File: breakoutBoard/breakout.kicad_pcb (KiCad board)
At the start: 2 copper layers, 62 x 106.9 mm, 9 parts, among them P1 CONN_02X50, P2 CONN_02X50, P3 CONN_02X50, P4 CONN_02X50, P7 CONN_02X30

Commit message: Basic pinout done and start of routing
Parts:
- added J1: Power_Breakout, Pin_Headers:Pin_Header_Straight_1x09_Pitch2.54mm, F.Cu at (84.0, 98.7)
- added J2: MIO_Breakout, Pin_Headers:Pin_Header_Straight_1x12_Pitch2.54mm, F.Cu at (84.3, 159.4)
- added J3: USB_OTG_Breakout, Pin_Headers:Pin_Header_Straight_1x06_Pitch2.54mm, F.Cu at (123.5, 65.7)
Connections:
- net /AD9361_AUXAC1 renamed Net-(P4-Pad7)
- net /AD9361_AUXAC2 renamed Net-(P4-Pad9)
- net /AD9361_AUXADC renamed Net-(P4-Pad8)
- net /AD9361_CLK renamed Net-(P4-Pad64)
- net /AD9361_GPO0 renamed Net-(P4-Pad2)
- net /AD9361_GPO1 renamed Net-(P4-Pad1)
- net /AD9361_GPO2 renamed Net-(P4-Pad4)
- net /AD9361_GPO3 renamed Net-(P4-Pad3)
- net /CAM_CLK_P renamed Net-(P1-Pad81)
- net /CAM_DATA0_P renamed Net-(P1-Pad54)
- net /CAM_DATA1_N renamed Net-(P1-Pad14)
- net /CAM_DATA2_N renamed Net-(P1-Pad13)
- net /CAM_DATA3_N renamed Net-(P1-Pad20)
- net /CAM_DATA4_N renamed Net-(P1-Pad19)
- net /CAM_DATA5_N renamed Net-(P1-Pad26)
- net /CAM_DATA6_N renamed Net-(P1-Pad25)
- net /CAM_GPIO_0 renamed Net-(P4-Pad20)
- net /CAM_GPIO_2 renamed Net-(P4-Pad19)
- net /CAM_GPIO_4 renamed Net-(P4-Pad26)
- net /CAM_GPIO_6 renamed Net-(P4-Pad25)
- net /CAM_GPIO_8 renamed Net-(P4-Pad32)
- net /CAM_REFCLK renamed Net-(P1-Pad82)
- net /CAM_SPI_CLK renamed Net-(P1-Pad31)
- net /CAM_SPI_MOSI renamed Net-(P1-Pad37)
- net /CAM_SYNC_P renamed Net-(P1-Pad47)
- net /CFG_INIT__B renamed Net-(P2-Pad10)
- net /CFG_VBATT renamed Net-(P1-Pad8)
- net /DIP_GPIO_1 renamed Net-(P4-Pad14)
- net /DIP_GPIO_3 renamed Net-(P2-Pad14)
- net /ET1_RXD3 renamed Net-(P4-Pad48)
- net /ETH0_MD1_N renamed Net-(P3-Pad54)
- net /ETH0_MD2_N renamed Net-(P3-Pad53)
- net /ETH0_PHY_LED0 renamed Net-(P3-Pad48)
- net /ETH0_PHY_LED1 renamed Net-(P3-Pad47)
- net /ETH1_RESETN renamed Net-(P4-Pad99)
- net /ETH1_RXD1 renamed Net-(P4-Pad43)
- net /ETH1_RX_CTRL renamed Net-(P4-Pad47)
- net /ETH1_TXD1 renamed Net-(P4-Pad53)
- net /ETH1_TX_CTRL renamed Net-(P4-Pad54)
- net /FAN_PWM renamed Net-(P4-Pad67)
- net /FAN_TACH renamed Net-(P4-Pad69)
- net /FMC_CLK0_M2C_N renamed Net-(P3-Pad94)
- net /FMC_CLK0_M2C_P renamed Net-(P3-Pad92)
- net /FMC_CLK1_M2C_N renamed Net-(P2-Pad44)
- net /FMC_CLK1_M2C_P renamed Net-(P2-Pad42)
- net /FMC_GBT_REFCLK_P renamed Net-(P1-Pad88)
- net /FMC_GBT_RX_P renamed Net-(P1-Pad87)
- net /FMC_GBT_TX_N renamed IO_00_33_JX1
- net /FMC_LA00_CC_N renamed Net-(P3-Pad87)
- net /FMC_LA01_CC_N renamed Net-(P3-Pad88)
- net /FMC_LA02_P renamed IO_L18_33_JX1_N
- net /FMC_LA03_P renamed Net-(P3-Pad26)
- net /FMC_LA04_P renamed IO_L20_33_JX1_N
- net /FMC_LA05_P renamed Net-(P3-Pad32)
- net /FMC_LA06_N renamed Net-(P3-Pad43)
- net /FMC_LA06_P renamed Net-(P3-Pad41)
- net /FMC_LA09_N renamed Net-(P3-Pad75)
- net /FMC_LA09_P renamed Net-(P3-Pad73)
- net /FMC_LA10_N renamed Net-(P3-Pad82)
- net /FMC_LA11_N renamed Net-(P3-Pad81)
- net /FMC_LA12_N renamed Net-(P3-Pad93)
- net /FMC_LA12_P renamed Net-(P3-Pad91)
- net /FMC_LA13_N renamed Net-(P3-Pad100)
- net /FMC_LA13_P renamed Net-(P3-Pad98)
- net /FMC_LA14_N renamed Net-(P3-Pad99)
- net /FMC_LA14_P renamed Net-(P3-Pad97)
- net /FMC_LA16_P renamed Net-(P2-Pad82)
- net /FMC_LA17_CC_N renamed Net-(P2-Pad37)
- net /FMC_LA17_CC_P renamed Net-(P2-Pad35)
- net /FMC_LA18_CC_N renamed Net-(P2-Pad38)
- net /FMC_LA18_CC_P renamed Net-(P2-Pad36)
- net /FMC_LA19_N renamed GPO_3
- net /FMC_LA19_P renamed GPO_1
- net /FMC_LA20_N renamed GPO_2
- net /FMC_LA20_P renamed GPO_0
- net /FMC_LA21_N renamed Net-(P2-Pad8)
- net /FMC_LA22_N renamed Net-(P2-Pad7)
- net /FMC_LA23_N renamed Net-(P2-Pad19)
- net /FMC_LA24_N renamed Net-(P2-Pad26)
- net /FMC_LA25_N renamed Net-(P2-Pad25)
- net /FMC_LA26_N renamed Net-(P2-Pad32)
- net /FMC_LA27_N renamed Net-(P2-Pad31)
- net /FMC_LA28_N renamed Net-(P2-Pad43)
- net /FMC_LA28_P renamed Net-(P2-Pad41)
- net /FMC_LA29_P renamed Net-(P2-Pad48)
- net /FMC_LA30_P renamed Net-(P2-Pad47)
- net /FMC_LA31_P renamed Net-(P2-Pad54)
- net /FMC_LA32_P renamed Net-(P2-Pad53)
- net /FMC_LA33_N renamed Net-(P2-Pad64)
- net /FMC_PRSNT renamed Net-(P2-Pad13)
- net /FPGA_TDI renamed Net-(P1-Pad3)
- net /FPGA_TDO renamed Net-(P1-Pad4)
- net /GPIO3 renamed Net-(P4-Pad88)
- net /HDMI_CLK renamed Net-(P1-Pad73)
- net /HDMI_D20 renamed Net-(P1-Pad41)
- net /HDMI_D21 renamed Net-(P1-Pad43)
- net /HDMI_D22 renamed Net-(P1-Pad48)
- net /HDMI_D24 renamed Net-(P1-Pad53)
- net /HDMI_D27 renamed Net-(P1-Pad64)
- net /HDMI_D34 renamed Net-(P1-Pad74)
- net /HDMI_D35 renamed Net-(P1-Pad76)
- net /HDMI_DE renamed Net-(P1-Pad75)
- net /HDMI_HSYNC renamed Net-(P1-Pad44)
- net /HDMI_PD renamed Net-(P1-Pad10)
- net /HDMI_SPDIF renamed Net-(P1-Pad36)
- net /HDMI_SPDIF_OUT renamed Net-(P1-Pad38)
- net /HDMI_VSYNC renamed Net-(P1-Pad42)
- net /I2C3_SCL renamed Net-(P2-Pad76)
- net /I2C3_SDA renamed Net-(P2-Pad74)
- net /I2S_LRCLK renamed Net-(P4-Pad36)
- net /I2S_MCLK renamed Net-(P4-Pad31)
- net /I2S_SDATA_IN renamed Net-(P4-Pad35)
- net /I2S_SDATA_OUT renamed Net-(P4-Pad38)
- net /JTAG_TCK renamed Net-(P1-Pad2)
- net /JTAG_TMS renamed Net-(P1-Pad1)
- net /LED_GPIO_0 renamed Net-(P4-Pad70)
- net /LED_GPIO_1 renamed Net-(P4-Pad13)
- net /MGTREFCLK1_N renamed JTAG_TDO
- net /MGTREFCLK1_P renamed JTAG_TCK
- net /MGTRX2_N renamed Net-(P1-Pad93)
- net /MGTRX2_P renamed Net-(P1-Pad91)
- net /MGTTX2_P renamed IO_L16_33_JX1_N
- net /PB_GPIO_1 renamed Net-(P4-Pad37)
- net /PB_GPIO_2 renamed Net-(P4-Pad42)
- net /PB_GPIO_3 renamed Net-(P4-Pad44)
- net /RF_GPIO1_BANK13 renamed Net-(P2-Pad63)
- net /RF_GPIO4_BANK34 renamed Net-(P4-Pad63)
- net /RF_GPIO5_BANK34 renamed Net-(P4-Pad68)
- net /SD1_B_CDN renamed Net-(P3-Pad42)
- net /SD1_B_CLK renamed Net-(P3-Pad44)
- net /SD1_B_DAT0 renamed Net-(P3-Pad38)
- net /SD1_B_DAT1 renamed IO_L01_33_JX1_P
- net /SD1_B_DAT3 renamed IO_L01_33_JX1_N
- net /SDA renamed Net-(P2-Pad20)
- net /SFP_GBT_RX_N renamed Net-(P1-Pad94)
- net /SFP_GBT_RX_P renamed Net-(P1-Pad92)
- net /SFP_GBT_TX_P renamed Net-(P3-Pad14)
- net /SGPIO1 renamed Net-(P4-Pad87)
- net /SGPIO3 renamed Net-(P4-Pad94)
- net /SGPIO_1 renamed Net-(P7-Pad25)
- net /SGPIO_3 renamed Net-(P7-Pad29)
- net /SGPIO_4 renamed Net-(P7-Pad32)
- net /SPI2_NSS renamed Net-(P4-Pad73)
- net /SYS_SPI_MISO renamed Net-(P4-Pad74)
- net /SYS_SPI_MOSI renamed Net-(P2-Pad75)
- net /SYS_SPI_NSS renamed Net-(P4-Pad76)
- net /SYS_SPI_SCK renamed Net-(P2-Pad73)
- net /USB_OTG_CPEN renamed Net-(P3-Pad69)
- net /USB_OTG_ID renamed Net-(P3-Pad64)
- net /USB_UART_RXD renamed Net-(P4-Pad100)
- net /USB_UART_TXD renamed Net-(P4-Pad97)
- net /USB_VBUS_OTG renamed Net-(P3-Pad67)
- net /VCCIO_EN renamed Net-(P2-Pad9)
- net Net-(P3-Pad2) renamed JTAG_TMS
- net Net-(P3-Pad4) renamed JTAG_TDI
- P1 pad 11: /CAM_DATA2_P -> JX_MGTAVCC
- P1 pad 12: /CAM_DATA1_P -> GND
- P1 pad 15: GND -> Net-(P1-Pad15)
- P1 pad 16: GND -> Net-(P1-Pad16)
- P1 pad 17: /CAM_DATA4_P -> GND
- P1 pad 18: /CAM_DATA3_P -> GND
- P1 pad 21: GND -> Net-(P1-Pad21)
- P1 pad 22: GND -> Net-(P1-Pad22)
- P1 pad 23: /CAM_DATA6_P -> GND
- P1 pad 24: /CAM_DATA5_P -> GND
- P1 pad 27: GND -> Net-(P1-Pad27)
- P1 pad 28: GND -> Net-(P1-Pad28)
- P1 pad 29: /CAM_SPI_EN -> GND
- P1 pad 30: /CAM_DATA7_P -> JX_MGTAVTT
- P1 pad 32: /CAM_DATA7_N -> JX_MGTAVTT
- P1 pad 33: GND -> Net-(P1-Pad33)
- P1 pad 34: GND -> Net-(P1-Pad34)
- P1 pad 35: /CAM_SPI_MISO -> GND
- P1 pad 39: GND -> Net-(P1-Pad39)
- P1 pad 45: GND -> JX_VCCO_13
- P1 pad 46: GND -> JX_VCCO_13
- P1 pad 49: /CAM_SYNC_N -> GND
- P1 pad 5: /RSTN_C2M -> JX_MGTAVCC
- P1 pad 50: /HDMI_D23 -> GND
- P1 pad 51: GND -> Net-(P1-Pad51)
- P1 pad 52: GND -> Net-(P1-Pad52)
- P1 pad 55: /HDMI_D25 -> GND
- P1 pad 56: /CAM_DATA0_N -> GND
- P1 pad 57: /VIN_HDR -> Net-(P1-Pad57)
- P1 pad 58: /VIN_HDR -> Net-(P1-Pad58)
- P1 pad 59: /VIN_HDR -> Net-(P1-Pad59)
- P1 pad 6: /PWR_ENABLE -> GND
- P1 pad 60: /VIN_HDR -> Net-(P1-Pad60)
- P1 pad 61: /HDMI_D28 -> GND
- P1 pad 62: /HDMI_D26 -> GND
- P1 pad 63: /HDMI_D29 -> USB_ID
- P1 pad 66: GND -> Net-(P1-Pad66)
- P1 pad 67: /HDMI_D32 -> USB_OTG_P
- P1 pad 68: /HDMI_D30 -> USB_VBUS_OTG
- P1 pad 69: /HDMI_D33 -> USB_OTG_N
- P1 pad 7: /CFG_DONE -> JX_MGTAVCC
- P1 pad 70: /HDMI_D31 -> USB_OTG_CPEN
- P1 pad 77: /VADJ -> GND
- P1 pad 79: /VADJ -> Net-(P1-Pad79)
- P1 pad 80: /VADJ -> Net-(P1-Pad80)
- P1 pad 83: /CAM_CLK_N -> GND
- P1 pad 84: /PB_GPIO_0 -> GND
- P1 pad 85: GND -> Net-(P1-Pad85)
- P1 pad 86: GND -> Net-(P1-Pad86)
- P1 pad 89: /FMC_GBT_RX_N -> GND
- P1 pad 9: /HDMI_INTN -> JX_MGTAVCC
- P1 pad 90: /FMC_GBT_REFCLK_N -> GND
- P2 pad 100: /DIP_GPIO_0 -> MIO51
- P2 pad 11: /VIN_HDR -> GND
- P2 pad 12: /PG_MODULE -> GND
- P2 pad 15: GND -> Net-(P2-Pad15)
- P2 pad 16: GND -> Net-(P2-Pad16)
- P2 pad 17: /FMC_LA23_P -> GND
- P2 pad 18: /SCL -> GND
- P2 pad 21: GND -> Net-(P2-Pad21)
- P2 pad 22: GND -> Net-(P2-Pad22)
- P2 pad 23: /FMC_LA25_P -> GND
- P2 pad 24: /FMC_LA24_P -> GND
- P2 pad 27: GND -> Net-(P2-Pad27)
- P2 pad 28: GND -> Net-(P2-Pad28)
- P2 pad 29: /FMC_LA27_P -> GND
- P2 pad 30: /FMC_LA26_P -> GND
- P2 pad 33: GND -> Net-(P2-Pad33)
- P2 pad 34: GND -> Net-(P2-Pad34)
- P2 pad 45: GND -> Net-(P2-Pad45)
- P2 pad 46: GND -> Net-(P2-Pad46)
- P2 pad 49: /FMC_LA30_N -> GND
- P2 pad 5: /FMC_LA22_P -> GND
- P2 pad 50: /FMC_LA29_N -> GND
- P2 pad 51: GND -> Net-(P2-Pad51)
- P2 pad 52: GND -> Net-(P2-Pad52)
- P2 pad 55: /FMC_LA32_N -> GND
- P2 pad 56: /FMC_LA31_N -> GND
- P2 pad 57: /VIN_HDR -> Net-(P2-Pad57)
- P2 pad 58: /VIN_HDR -> Net-(P2-Pad58)
- P2 pad 59: /VIN_HDR -> Net-(P2-Pad59)
- P2 pad 6: /FMC_LA21_P -> GND
- P2 pad 60: /VIN_HDR -> Net-(P2-Pad60)
- P2 pad 61: /RF_GPIO0_BANK13 -> GND
- P2 pad 62: /FMC_LA33_P -> GND
- P2 pad 67: /I2C2_SDA -> Net-(P2-Pad67)
- P2 pad 68: /I2C2_SDA -> Net-(P2-Pad68)
- P2 pad 69: /I2C2_SCL -> Net-(P2-Pad69)
- P2 pad 70: /I2C2_SCL -> Net-(P2-Pad70)
- P2 pad 77: /1V8 -> Net-(P2-Pad77)
- P2 pad 78: GND -> Net-(P2-Pad78)
- P2 pad 79: /1V8 -> Net-(P2-Pad79)
- P2 pad 80: /1V8 -> Net-(P2-Pad80)
- P2 pad 81: /FMC_LA15_P -> 3V3_I2C
- P2 pad 83: /FMC_LA15_N -> GND
- P2 pad 84: /FMC_LA16_N -> GND
- P2 pad 85: GND -> MIO15
- P2 pad 86: GND -> MIO12
- P2 pad 87: /SFP_GPIO_0 -> MIO10
- P2 pad 88: /SFP_GPIO_2 -> MIO11
- P2 pad 89: /SFP_GPIO_1 -> GND
- P2 pad 90: /SFP_GPIO_3 -> GND
- P2 pad 91: GND -> MIO13
- P2 pad 92: GND -> MIO46
- P2 pad 93: /SFP_GPIO_6 -> MIO14
- P2 pad 94: /SFP_GPIO_4 -> MIO47
- P2 pad 95: /RF_GPIO2_BANK12 -> GND
- P2 pad 96: /SFP_GPIO_5 -> GND
- P2 pad 97: /VADJ -> MIO0
- P2 pad 98: /LED_GPIO_3 -> MIO49
- P2 pad 99: Net-(P2-Pad99) -> MIO48
- P3 pad 10: /1V0_AVCC -> Net-(P3-Pad10)
- P3 pad 11: GND -> IO_L16_33_JX1_P
- P3 pad 12: /1V0_AVCC -> Net-(P3-Pad12)
- P3 pad 15: /MGTTX2_N -> GND
- P3 pad 16: /SFP_GBT_TX_N -> GND
- P3 pad 17: GND -> IO_L18_33_JX1_P
- P3 pad 18: GND -> Net-(P3-Pad18)
- P3 pad 21: /FMC_LA02_N -> GND
- P3 pad 22: Net-(P3-Pad22) -> GND
- P3 pad 23: GND -> IO_L20_33_JX1_P
- P3 pad 24: GND -> Net-(P3-Pad24)
- P3 pad 27: /FMC_LA04_N -> GND
- P3 pad 28: /FMC_LA03_N -> GND
- P3 pad 29: /1V2_AVTT -> IO_L22_33_JX1_P
- P3 pad 30: GND -> Net-(P3-Pad30)
- P3 pad 31: /1V2_AVTT -> IO_L22_33_JX1_N
- P3 pad 33: /SD1_B_CMD -> GND
- P3 pad 34: /FMC_LA05_N -> GND
- P3 pad 36: GND -> Net-(P3-Pad36)
- P3 pad 40: /SD1_B_DAT2 -> GND
- P3 pad 45: /VADJ -> GND
- P3 pad 46: /VADJ -> GND
- P3 pad 49: GND -> Net-(P3-Pad49)
- P3 pad 5: GND -> PWR_ENABLE
- P3 pad 50: GND -> Net-(P3-Pad50)
- P3 pad 51: /ETH0_MD2_P -> GND
- P3 pad 52: /ETH0_MD1_P -> GND
- P3 pad 55: GND -> Net-(P3-Pad55)
- P3 pad 56: GND -> Net-(P3-Pad56)
- P3 pad 57: /ETH0_MD4_P -> +5V
- P3 pad 58: /ETH0_MD3_P -> +5V
- P3 pad 59: /ETH0_MD4_N -> +5V
- P3 pad 6: /1V0_AVCC -> Carrier_Reset
- P3 pad 60: /ETH0_MD3_N -> +5V
- P3 pad 61: GND -> Net-(P3-Pad61)
- P3 pad 62: GND -> Net-(P3-Pad62)
- P3 pad 63: /FMC_LA07_P -> Net-(P3-Pad63)
- P3 pad 65: /FMC_LA07_P -> GND
- P3 pad 68: /FMC_LA08_P -> Net-(P3-Pad68)
- P3 pad 7: /FMC_GBT_TX_P -> FPGA_VBATT
- P3 pad 70: /FMC_LA08_N -> Net-(P3-Pad70)
- P3 pad 74: /FMC_LA08_P -> Net-(P3-Pad74)
- P3 pad 76: /FMC_LA08_N -> Net-(P3-Pad76)
- P3 pad 78: GND -> JX_VCCO_12
- P3 pad 79: /FMC_LA11_P -> JX_VCCO_12
- P3 pad 8: /1V0_AVCC -> Net-(P3-Pad8)
- P3 pad 80: /FMC_LA10_P -> JX_VCCO_12
- P3 pad 83: GND -> Net-(P3-Pad83)
- P3 pad 84: GND -> Net-(P3-Pad84)
- P3 pad 85: /FMC_LA00_CC_P -> GND
- P3 pad 86: /FMC_LA01_CC_P -> GND
- P3 pad 89: GND -> Net-(P3-Pad89)
- P3 pad 90: GND -> Net-(P3-Pad90)
- P4 pad 11: GND -> Net-(P4-Pad11)
- P4 pad 12: GND -> +5V
- P4 pad 15: /LED_GPIO_2 -> GND
- P4 pad 16: /DIP_GPIO_2 -> GND
- P4 pad 17: GND -> Net-(P4-Pad17)
- P4 pad 18: GND -> Net-(P4-Pad18)
- P4 pad 21: /CAM_GPIO_3 -> GND
- P4 pad 22: /CAM_GPIO_1 -> GND
- P4 pad 23: GND -> Net-(P4-Pad23)
- P4 pad 24: GND -> Net-(P4-Pad24)
- P4 pad 27: /CAM_GPIO_7 -> GND
- P4 pad 28: /CAM_GPIO_5 -> GND
- P4 pad 29: GND -> Net-(P4-Pad29)
- P4 pad 30: GND -> Net-(P4-Pad30)
- P4 pad 33: /I2S_BCLK -> GND
- P4 pad 34: /RF_GPIO3_BANK34 -> GND
- P4 pad 41: /ETH1_RX_CLK -> Net-(P4-Pad41)
- P4 pad 45: /ETH1_RX_CLK -> GND
- P4 pad 46: /ETH1_RXD2 -> GND
- P4 pad 49: GND -> Net-(P4-Pad49)
- P4 pad 5: GND -> Net-(P4-Pad5)
- P4 pad 50: GND -> Net-(P4-Pad50)
- P4 pad 51: /ETH1_TXD0 -> GND
- P4 pad 52: /ETH1_TX_CLK -> GND
- P4 pad 55: GND -> Net-(P4-Pad55)
- P4 pad 56: GND -> Net-(P4-Pad56)
- P4 pad 57: /ETH1_MDC -> +5V
- P4 pad 58: /ETH1_TXD2 -> +5V
- P4 pad 59: /ETH1_MDIO -> +5V
- P4 pad 6: GND -> Net-(P4-Pad6)
- P4 pad 60: /EHT1_TXD3 -> +5V
- P4 pad 61: GND -> Net-(P4-Pad61)
- P4 pad 62: GND -> Net-(P4-Pad62)
- P4 pad 75: /SPI2_MISO -> Net-(P4-Pad75)
- P4 pad 77: /GPIO0 -> GND
- P4 pad 78: /SPI2_SCK -> JX_VCCO_33_34
- P4 pad 79: /GPIO1 -> JX_VCCO_33_34
- P4 pad 80: /SPI2_MOSI -> JX_VCCO_33_34
- P4 pad 83: GND -> Net-(P4-Pad83)
- P4 pad 84: GND -> Net-(P4-Pad84)
- P4 pad 85: /SGPIO0 -> GND
- P4 pad 86: /GPIO2 -> GND
- P4 pad 89: GND -> Net-(P4-Pad89)
- P4 pad 90: GND -> Net-(P4-Pad90)
- P4 pad 91: /SYS_SDA -> GND
- P4 pad 92: /SGPIO2 -> GND
- P4 pad 93: /SYS_SCL -> Net-(P4-Pad93)
- P4 pad 95: GND -> Net-(P4-Pad95)
- P4 pad 96: GND -> Net-(P4-Pad96)
- P4 pad 98: Net-(P4-Pad98) -> JX_VCCO_13
- P7 pad 1: GND -> +5V
- P7 pad 10: /SYS_SDA -> GND
- P7 pad 11: +3V3 -> Net-(P7-Pad11)
- P7 pad 13: GND -> Net-(P7-Pad13)
- P7 pad 14: +3V3 -> GND
- P7 pad 15: /SPI2_MISO -> Net-(P7-Pad15)
- P7 pad 17: GND -> +5V
- P7 pad 18: /SPI2_MOSI -> GND
- P7 pad 19: /SPI2_SCK -> Net-(P7-Pad19)
- P7 pad 2: +3V3 -> GND
- P7 pad 22: Net-(P7-Pad22) -> GND
- P7 pad 23: GND -> Net-(P7-Pad23)
- P7 pad 24: /SGPIO_0 -> GND
- P7 pad 27: GND -> Net-(P7-Pad27)
- P7 pad 28: /SGPIO_2 -> GND
- P7 pad 3: +5V -> PWR_ENABLE
- P7 pad 33: +3V3 -> GND
- P7 pad 34: GND -> MIO0
- P7 pad 36: +3V3 -> MIO48
- P7 pad 37: /SYS_MISO -> GND
- P7 pad 38: GND -> MIO10
- P7 pad 40: /SYS_MOSI -> MIO14
- P7 pad 41: /SYS_SCK -> GND
- P7 pad 42: GND -> MIO13
- P7 pad 44: /GPIO_7 -> +5V
- P7 pad 45: /GPIO_8 -> GND
- P7 pad 46: GND -> MIO15
- P7 pad 48: /GPIO_9 -> MIO51
- P7 pad 49: /GPIO_10 -> GND
- P7 pad 5: GND -> Net-(P7-Pad5)
- P7 pad 50: GND -> MIO49
- P7 pad 52: /GPIO_11 -> MIO47
- P7 pad 53: +3V3 -> GND
- P7 pad 54: GND -> MIO46
- P7 pad 56: +3V3 -> MIO11
- P7 pad 57: +5V -> GND
- P7 pad 58: GND -> MIO12
- P7 pad 6: +12V -> GND
- P7 pad 60: +12V -> +5V
- P7 pad 7: /SYS_SCL -> Net-(P7-Pad7)
- P7 pad 9: GND -> Net-(P7-Pad9)
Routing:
- net Net-(P3-Pad74): track 0.00 -> 0.93 mm
- net GND: track 0.00 -> 0.93 mm
- net /SD1_B_DAT2: track 0.93 -> 0.00 mm
- net /FMC_LA08_P: track 0.93 -> 0.00 mm
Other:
- board size 62 x 106.9 mm -> 78.5 x 106.9 mm

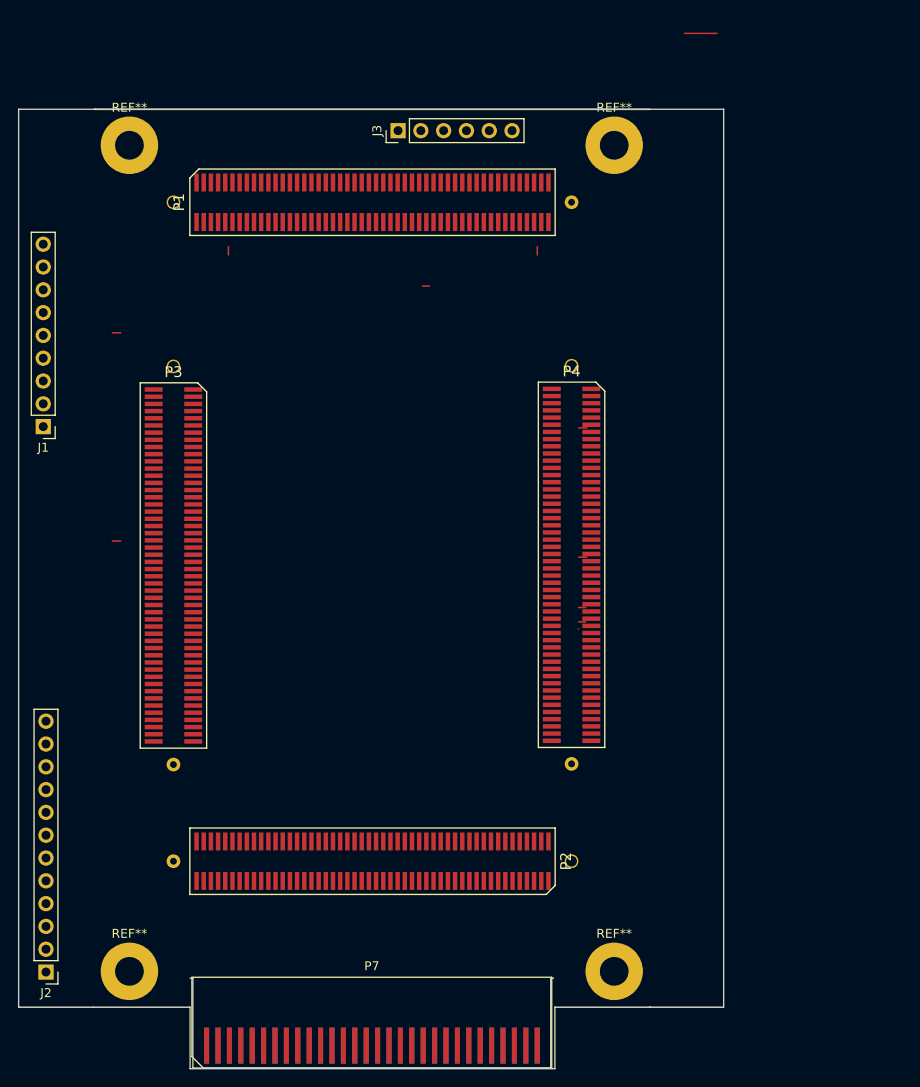
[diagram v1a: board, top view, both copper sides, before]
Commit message: Added zones
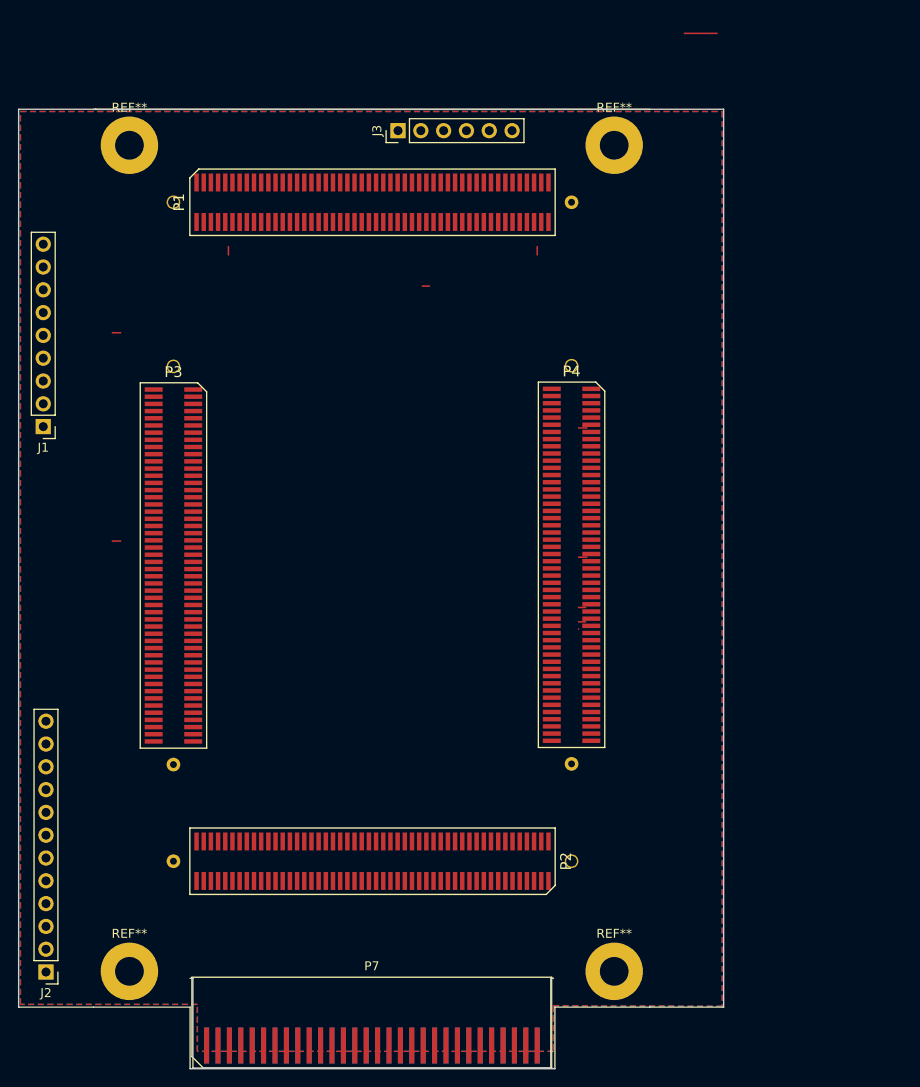
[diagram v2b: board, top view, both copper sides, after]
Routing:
- added copper zone on B.Cu, net +5V
- added copper zone on F.Cu, net GND
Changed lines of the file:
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@@
   (general
     (links 194)
-    (no_connects 194)
+    (no_connects 178)
     (area 89.510799 63.247199 151.636801 170.255001)
     (thickness 1.6)
@@
   (segment (start 97 111.4) (end 96.011767 111.4) (width 0.1778) (layer F.Cu) (net 184))
   (segment (start 96.069938 123.4) (end 97 123.4) (width 0.1778) (layer F.Cu) (net 202))
+  (zone (net 5) (net_name GND) (layer F.Cu) (hatch edge 0.508)
+    (connect_pads (clearance 0.508))
+    (min_thickness 0.254)
+    (fill yes (arc_segments 16) (thermal_gap 0.508) (thermal_bridge_width 0.508))
+    (polygon
+      (pts
+        (xy 159.6136 163.2204) (xy 140.8176 163.1696) (xy 140.8176 168.2496) (xy 101.1428 168.2496) (xy 101.1428 163.0172)
+        (xy 81.4324 163.0172) (xy 81.4324 63.5508) (xy 159.6136 63.5508)
+      )
+    )
+  )
+  (zone (net 10) (net_name +5V) (layer B.Cu) (hatch edge 0.508)
+    (connect_pads (clearance 0.508))
+    (min_thickness 0.254)
+    (fill yes (arc_segments 16) (thermal_gap 0.508) (thermal_bridge_width 0.508))
+    (polygon
+      (pts
+        (xy 159.6136 163.2204) (xy 140.8176 163.1696) (xy 140.8176 168.2496) (xy 101.1428 168.2496) (xy 101.1428 163.0172)
+        (xy 81.4324 163.0172) (xy 81.4324 63.5508) (xy 159.6136 63.5508)
+      )
+    )
+  )
 )

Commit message: Started routing
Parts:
- J1: footprint Pin_Headers:Pin_Header_Straight_1x09_Pitch2.54mm -> Pin_Headers:Pin_Header_Straight_1x10_Pitch2.54mm
- moved J2 28.2 mm to (84.9, 131.3), turned to 0 degrees
- moved J1 2.44 mm to (83.9, 101.1)
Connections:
- J2 pad 1: MIO15 -> MIO12
- J2 pad 10: MIO46 -> MIO14
- J2 pad 11: MIO11 -> MIO0
- J2 pad 12: MIO12 -> MIO48
- J2 pad 2: MIO10 -> MIO11
- J2 pad 3: MIO13 -> MIO46
- J2 pad 4: MIO14 -> MIO47
- J2 pad 5: MIO0 -> MIO49
- J2 pad 6: MIO48 -> MIO51
- J2 pad 7: MIO51 -> MIO15
- J2 pad 8: MIO49 -> MIO10
- J2 pad 9: MIO47 -> MIO13
- P7 pad 10: GND -> MIO49
- P7 pad 11: Net-(P7-Pad11) -> GND
- P7 pad 13: Net-(P7-Pad13) -> MIO14
- P7 pad 14: GND -> MIO47
- P7 pad 15: Net-(P7-Pad15) -> GND
- P7 pad 17: +5V -> MIO13
- P7 pad 18: GND -> MIO46
- P7 pad 19: Net-(P7-Pad19) -> GND
- P7 pad 2: GND -> +5V
- P7 pad 21: Net-(P7-Pad21) -> MIO10
- P7 pad 22: GND -> MIO11
- P7 pad 23: Net-(P7-Pad23) -> GND
- P7 pad 25: Net-(P7-Pad25) -> MIO15
- P7 pad 26: GND -> MIO12
- P7 pad 27: Net-(P7-Pad27) -> GND
- P7 pad 3: PWR_ENABLE -> GND
- P7 pad 30: GND -> Net-(P7-Pad30)
- P7 pad 32: Net-(P7-Pad32) -> GND
- P7 pad 33: GND -> +5V
- P7 pad 34: MIO0 -> +5V
- P7 pad 36: MIO48 -> GND
- P7 pad 37: GND -> Net-(P7-Pad37)
- P7 pad 38: MIO10 -> Net-(P7-Pad38)
- P7 pad 40: MIO14 -> GND
- P7 pad 41: GND -> Net-(P7-Pad41)
- P7 pad 42: MIO13 -> Net-(P7-Pad42)
- P7 pad 44: +5V -> GND
- P7 pad 45: GND -> Net-(P7-Pad45)
- P7 pad 46: MIO15 -> Net-(P7-Pad46)
- P7 pad 48: MIO51 -> GND
- P7 pad 49: GND -> Net-(P7-Pad49)
- P7 pad 5: Net-(P7-Pad5) -> MIO48
- P7 pad 50: MIO49 -> Net-(P7-Pad50)
- P7 pad 52: MIO47 -> GND
- P7 pad 53: GND -> Net-(P7-Pad53)
- P7 pad 54: MIO46 -> Net-(P7-Pad54)
- P7 pad 56: MIO11 -> GND
- P7 pad 57: GND -> PWR_ENABLE
- P7 pad 58: MIO12 -> Net-(P7-Pad58)
- P7 pad 6: GND -> MIO51
- P7 pad 60: +5V -> GND
- P7 pad 7: Net-(P7-Pad7) -> GND
- P7 pad 9: Net-(P7-Pad9) -> MIO0
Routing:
- net MIO12: track 0.00 -> 55.7 mm, vias 0 -> 1
- net MIO11: track 0.00 -> 53.2 mm, vias 0 -> 1
- net MIO46: track 0.00 -> 50.3 mm, vias 0 -> 1
- net MIO47: track 0.00 -> 47.2 mm, vias 0 -> 1
- net MIO15: track 0.00 -> 47.2 mm
- net MIO10: track 0.00 -> 46.4 mm
- net MIO13: track 0.00 -> 44.5 mm
- net MIO49: track 0.00 -> 44.2 mm, vias 0 -> 1
- net MIO14: track 0.00 -> 43.6 mm
- net MIO0: track 0.00 -> 42.3 mm
- net MIO51: track 0.00 -> 40.8 mm, vias 0 -> 1
- net MIO48: track 0.00 -> 37.6 mm
- net GND: track 0.93 -> 16.7 mm

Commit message: Work on schematic and traces
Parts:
- added J4: Cardedge breakout, Pin_Headers:Pin_Header_Straight_1x17_Pitch2.54mm, F.Cu at (176.8, 158.4)
- added P5: CONN_02X30, Connectors_Samtec:MECF-30-01-L-DV-WT_Socket, F.Cu at (163.9, 138.5)
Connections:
- net Net-(P2-Pad10) renamed AUXDAC2
- net Net-(P2-Pad7) renamed AUXADC
- net Net-(P2-Pad8) renamed AUXDAC1
- net Net-(P2-Pad9) renamed VDDA_GPO_PWR
- net Net-(P4-Pad10) renamed PG_1P8V
- P1 pad 1: Net-(P1-Pad1) -> GND
- P1 pad 10: Net-(P1-Pad10) -> GND
- P1 pad 100: Net-(P1-Pad100) -> GND
- P1 pad 13: Net-(P1-Pad13) -> GND
- P1 pad 14: Net-(P1-Pad14) -> GND
- P1 pad 15: Net-(P1-Pad15) -> GND
- P1 pad 16: Net-(P1-Pad16) -> GND
- P1 pad 19: Net-(P1-Pad19) -> GND
- P1 pad 2: Net-(P1-Pad2) -> GND
- P1 pad 20: Net-(P1-Pad20) -> GND
- P1 pad 21: Net-(P1-Pad21) -> GND
- P1 pad 22: Net-(P1-Pad22) -> GND
- P1 pad 25: Net-(P1-Pad25) -> GND
- P1 pad 26: Net-(P1-Pad26) -> GND
- P1 pad 27: Net-(P1-Pad27) -> GND
- P1 pad 28: Net-(P1-Pad28) -> GND
- P1 pad 3: Net-(P1-Pad3) -> GND
- P1 pad 31: Net-(P1-Pad31) -> GND
- P1 pad 33: Net-(P1-Pad33) -> GND
- P1 pad 34: Net-(P1-Pad34) -> GND
- P1 pad 36: Net-(P1-Pad36) -> GND
- P1 pad 37: Net-(P1-Pad37) -> GND
- P1 pad 38: Net-(P1-Pad38) -> GND
- P1 pad 39: Net-(P1-Pad39) -> GND
- P1 pad 4: Net-(P1-Pad4) -> GND
- P1 pad 41: Net-(P1-Pad41) -> GND
- P1 pad 42: Net-(P1-Pad42) -> GND
- P1 pad 43: Net-(P1-Pad43) -> GND
- P1 pad 44: Net-(P1-Pad44) -> GND
- P1 pad 47: Net-(P1-Pad47) -> GND
- P1 pad 48: Net-(P1-Pad48) -> GND
- P1 pad 51: Net-(P1-Pad51) -> GND
- P1 pad 52: Net-(P1-Pad52) -> GND
- P1 pad 53: Net-(P1-Pad53) -> GND
- P1 pad 54: Net-(P1-Pad54) -> GND
- P1 pad 57: Net-(P1-Pad57) -> GND
- P1 pad 58: Net-(P1-Pad58) -> GND
- P1 pad 59: Net-(P1-Pad59) -> GND
- P1 pad 60: Net-(P1-Pad60) -> GND
- P1 pad 64: Net-(P1-Pad64) -> GND
- P1 pad 66: Net-(P1-Pad66) -> GND
- P1 pad 73: Net-(P1-Pad73) -> GND
- P1 pad 74: Net-(P1-Pad74) -> GND
- P1 pad 75: Net-(P1-Pad75) -> GND
- P1 pad 76: Net-(P1-Pad76) -> GND
- P1 pad 79: Net-(P1-Pad79) -> GND
- P1 pad 8: Net-(P1-Pad8) -> GND
- P1 pad 80: Net-(P1-Pad80) -> GND
- P1 pad 81: Net-(P1-Pad81) -> GND
- P1 pad 82: Net-(P1-Pad82) -> GND
- P1 pad 85: Net-(P1-Pad85) -> GND
- P1 pad 86: Net-(P1-Pad86) -> GND
- P1 pad 87: Net-(P1-Pad87) -> GND
- P1 pad 88: Net-(P1-Pad88) -> GND
- P1 pad 91: Net-(P1-Pad91) -> GND
- P1 pad 92: Net-(P1-Pad92) -> GND
- P1 pad 93: Net-(P1-Pad93) -> GND
- P1 pad 94: Net-(P1-Pad94) -> GND
- P1 pad 97: Net-(P1-Pad97) -> GND
- P1 pad 98: Net-(P1-Pad98) -> GND
- P1 pad 99: Net-(P1-Pad99) -> GND
- P2 pad 13: Net-(P2-Pad13) -> GND
- P2 pad 14: Net-(P2-Pad14) -> GND
- P2 pad 15: Net-(P2-Pad15) -> GND
- P2 pad 16: Net-(P2-Pad16) -> GND
- P2 pad 19: Net-(P2-Pad19) -> GND
- P2 pad 20: Net-(P2-Pad20) -> GND
- P2 pad 21: Net-(P2-Pad21) -> GND
- P2 pad 22: Net-(P2-Pad22) -> GND
- P2 pad 25: Net-(P2-Pad25) -> GND
- P2 pad 26: Net-(P2-Pad26) -> GND
- P2 pad 27: Net-(P2-Pad27) -> GND
- P2 pad 28: Net-(P2-Pad28) -> GND
- P2 pad 31: Net-(P2-Pad31) -> GND
- P2 pad 32: Net-(P2-Pad32) -> GND
- P2 pad 33: Net-(P2-Pad33) -> GND
- P2 pad 34: Net-(P2-Pad34) -> GND
- P2 pad 35: Net-(P2-Pad35) -> GND
- P2 pad 36: Net-(P2-Pad36) -> GND
- P2 pad 37: Net-(P2-Pad37) -> GND
- P2 pad 38: Net-(P2-Pad38) -> GND
- P2 pad 41: Net-(P2-Pad41) -> GND
- P2 pad 42: Net-(P2-Pad42) -> GND
- P2 pad 43: Net-(P2-Pad43) -> GND
- P2 pad 44: Net-(P2-Pad44) -> GND
- P2 pad 45: Net-(P2-Pad45) -> GND
- P2 pad 46: Net-(P2-Pad46) -> GND
- P2 pad 47: Net-(P2-Pad47) -> GND
- P2 pad 48: Net-(P2-Pad48) -> GND
- P2 pad 51: Net-(P2-Pad51) -> GND
- P2 pad 52: Net-(P2-Pad52) -> GND
- P2 pad 53: Net-(P2-Pad53) -> GND
- P2 pad 54: Net-(P2-Pad54) -> GND
- P2 pad 57: Net-(P2-Pad57) -> GND
- P2 pad 58: Net-(P2-Pad58) -> GND
- P2 pad 59: Net-(P2-Pad59) -> GND
- P2 pad 60: Net-(P2-Pad60) -> GND
- P2 pad 63: Net-(P2-Pad63) -> GND
- P2 pad 64: Net-(P2-Pad64) -> GND
- P2 pad 67: Net-(P2-Pad67) -> GND
- P2 pad 68: Net-(P2-Pad68) -> GND
- P2 pad 69: Net-(P2-Pad69) -> GND
- P2 pad 70: Net-(P2-Pad70) -> GND
- P2 pad 73: Net-(P2-Pad73) -> GND
- P2 pad 74: Net-(P2-Pad74) -> GND
- P2 pad 75: Net-(P2-Pad75) -> GND
- P2 pad 76: Net-(P2-Pad76) -> GND
- P2 pad 77: Net-(P2-Pad77) -> GND
- P2 pad 78: Net-(P2-Pad78) -> GND
- P2 pad 79: Net-(P2-Pad79) -> GND
- P2 pad 80: Net-(P2-Pad80) -> GND
- P3 pad 10: Net-(P3-Pad10) -> GND
- P3 pad 100: Net-(P3-Pad100) -> GND
- P3 pad 12: Net-(P3-Pad12) -> GND
- P3 pad 14: Net-(P3-Pad14) -> GND
- P3 pad 18: Net-(P3-Pad18) -> GND
- P3 pad 20: Net-(P3-Pad20) -> GND
- P3 pad 24: Net-(P3-Pad24) -> GND
- P3 pad 26: Net-(P3-Pad26) -> GND
- P3 pad 30: Net-(P3-Pad30) -> GND
- P3 pad 32: Net-(P3-Pad32) -> GND
- P3 pad 36: Net-(P3-Pad36) -> GND
- P3 pad 38: Net-(P3-Pad38) -> GND
- P3 pad 41: Net-(P3-Pad41) -> GND
- P3 pad 42: Net-(P3-Pad42) -> GND
- P3 pad 43: Net-(P3-Pad43) -> GND
- P3 pad 44: Net-(P3-Pad44) -> GND
- P3 pad 47: Net-(P3-Pad47) -> GND
- P3 pad 48: Net-(P3-Pad48) -> GND
- P3 pad 49: Net-(P3-Pad49) -> GND
- P3 pad 50: Net-(P3-Pad50) -> GND
- P3 pad 53: Net-(P3-Pad53) -> GND
- P3 pad 54: Net-(P3-Pad54) -> GND
- P3 pad 55: Net-(P3-Pad55) -> GND
- P3 pad 56: Net-(P3-Pad56) -> GND
- P3 pad 61: Net-(P3-Pad61) -> GND
- P3 pad 62: Net-(P3-Pad62) -> GND
- P3 pad 63: Net-(P3-Pad63) -> GND
- P3 pad 64: Net-(P3-Pad64) -> GND
- P3 pad 67: Net-(P3-Pad67) -> GND
- P3 pad 68: Net-(P3-Pad68) -> GND
- P3 pad 69: Net-(P3-Pad69) -> GND
- P3 pad 70: Net-(P3-Pad70) -> GND
- P3 pad 73: Net-(P3-Pad73) -> GND
- P3 pad 74: Net-(P3-Pad74) -> GND
- P3 pad 75: Net-(P3-Pad75) -> GND
- P3 pad 76: Net-(P3-Pad76) -> GND
- P3 pad 8: Net-(P3-Pad8) -> FPGA_DONE
- P3 pad 81: Net-(P3-Pad81) -> GND
- P3 pad 82: Net-(P3-Pad82) -> GND
- P3 pad 83: Net-(P3-Pad83) -> GND
- P3 pad 84: Net-(P3-Pad84) -> GND
- P3 pad 87: Net-(P3-Pad87) -> GND
- P3 pad 88: Net-(P3-Pad88) -> GND
- P3 pad 89: Net-(P3-Pad89) -> GND
- P3 pad 90: Net-(P3-Pad90) -> GND
- P3 pad 91: Net-(P3-Pad91) -> GND
- P3 pad 92: Net-(P3-Pad92) -> GND
- P3 pad 93: Net-(P3-Pad93) -> GND
- P3 pad 94: Net-(P3-Pad94) -> GND
- P3 pad 97: Net-(P3-Pad97) -> GND
- P3 pad 98: Net-(P3-Pad98) -> GND
- P3 pad 99: Net-(P3-Pad99) -> GND
- P4 pad 1: Net-(P4-Pad1) -> GND
- P4 pad 100: Net-(P4-Pad100) -> GND
- P4 pad 11: Net-(P4-Pad11) -> PG_MODULE
- P4 pad 13: Net-(P4-Pad13) -> GND
- P4 pad 14: Net-(P4-Pad14) -> GND
- P4 pad 17: Net-(P4-Pad17) -> GND
- P4 pad 18: Net-(P4-Pad18) -> GND
- P4 pad 19: Net-(P4-Pad19) -> GND
- P4 pad 2: Net-(P4-Pad2) -> GND
- P4 pad 20: Net-(P4-Pad20) -> GND
- P4 pad 23: Net-(P4-Pad23) -> GND
- P4 pad 24: Net-(P4-Pad24) -> GND
- P4 pad 25: Net-(P4-Pad25) -> GND
- P4 pad 26: Net-(P4-Pad26) -> GND
- P4 pad 29: Net-(P4-Pad29) -> GND
- P4 pad 3: Net-(P4-Pad3) -> GND
- P4 pad 30: Net-(P4-Pad30) -> GND
- P4 pad 31: Net-(P4-Pad31) -> GND
- P4 pad 32: Net-(P4-Pad32) -> GND
- P4 pad 35: Net-(P4-Pad35) -> GND
- P4 pad 36: Net-(P4-Pad36) -> GND
- P4 pad 37: Net-(P4-Pad37) -> GND
- P4 pad 38: Net-(P4-Pad38) -> GND
- P4 pad 4: Net-(P4-Pad4) -> GND
- P4 pad 41: Net-(P4-Pad41) -> GND
- P4 pad 42: Net-(P4-Pad42) -> GND
- P4 pad 43: Net-(P4-Pad43) -> GND
- P4 pad 44: Net-(P4-Pad44) -> GND
- P4 pad 47: Net-(P4-Pad47) -> GND
- P4 pad 48: Net-(P4-Pad48) -> GND
- P4 pad 49: Net-(P4-Pad49) -> GND
- P4 pad 5: Net-(P4-Pad5) -> GND
- P4 pad 50: Net-(P4-Pad50) -> GND
- P4 pad 53: Net-(P4-Pad53) -> GND
- P4 pad 54: Net-(P4-Pad54) -> GND
- P4 pad 55: Net-(P4-Pad55) -> GND
- P4 pad 56: Net-(P4-Pad56) -> GND
- P4 pad 6: Net-(P4-Pad6) -> GND
- P4 pad 61: Net-(P4-Pad61) -> GND
- P4 pad 62: Net-(P4-Pad62) -> GND
- P4 pad 63: Net-(P4-Pad63) -> GND
- P4 pad 64: Net-(P4-Pad64) -> GND
- P4 pad 67: Net-(P4-Pad67) -> GND
- P4 pad 68: Net-(P4-Pad68) -> GND
- P4 pad 69: Net-(P4-Pad69) -> GND
- P4 pad 7: Net-(P4-Pad7) -> GND
- P4 pad 70: Net-(P4-Pad70) -> GND
- P4 pad 73: Net-(P4-Pad73) -> GND
- P4 pad 74: Net-(P4-Pad74) -> GND
- P4 pad 75: Net-(P4-Pad75) -> GND
- P4 pad 76: Net-(P4-Pad76) -> GND
- P4 pad 8: Net-(P4-Pad8) -> GND
- P4 pad 81: Net-(P4-Pad81) -> GND
- P4 pad 82: Net-(P4-Pad82) -> GND
- P4 pad 83: Net-(P4-Pad83) -> GND
- P4 pad 84: Net-(P4-Pad84) -> GND
- P4 pad 87: Net-(P4-Pad87) -> GND
- P4 pad 88: Net-(P4-Pad88) -> GND
- P4 pad 89: Net-(P4-Pad89) -> GND
- P4 pad 9: Net-(P4-Pad9) -> GND
- P4 pad 90: Net-(P4-Pad90) -> GND
- P4 pad 93: Net-(P4-Pad93) -> GND
- P4 pad 94: Net-(P4-Pad94) -> GND
- P4 pad 95: Net-(P4-Pad95) -> GND
- P4 pad 96: Net-(P4-Pad96) -> GND
- P4 pad 97: Net-(P4-Pad97) -> GND
- P4 pad 99: Net-(P4-Pad99) -> GND
- P7 pad 1: +5V -> GND
- P7 pad 2: +5V -> GND
- P7 pad 21: MIO10 -> Net-(P7-Pad21)
- P7 pad 22: MIO11 -> Net-(P7-Pad22)
- P7 pad 25: MIO15 -> MIO10
- P7 pad 26: MIO12 -> MIO11
- P7 pad 29: Net-(P7-Pad29) -> MIO15
- P7 pad 30: Net-(P7-Pad30) -> MIO12
- P7 pad 37: Net-(P7-Pad37) -> +5V
- P7 pad 38: Net-(P7-Pad38) -> +5V
- P7 pad 53: Net-(P7-Pad53) -> PG_MODULE
- P7 pad 58: Net-(P7-Pad58) -> FPGA_DONE
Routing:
- net Net-(P7-Pad22): track 0.00 -> 25.7 mm
- net MIO0: track 42.3 -> 63.1 mm
- net MIO14: track 43.6 -> 64.1 mm
- net MIO48: track 37.6 -> 57.9 mm
- net Net-(P7-Pad21): track 0.00 -> 20.2 mm
- net MIO13: track 44.5 -> 64.5 mm
- net MIO11: track 53.2 -> 69.8 mm, vias 1 -> 2
- net FPGA_DONE: track 0.00 -> 15.2 mm, vias 0 -> 1
- net MIO46: track 50.3 -> 65.2 mm, vias 1 -> 2
- net MIO47: track 47.2 -> 62.0 mm, vias 1 -> 2
- net MIO49: track 44.2 -> 59.0 mm, vias 1 -> 2
- net MIO51: track 40.8 -> 55.6 mm, vias 1 -> 2
- net PWR_ENABLE: track 0.00 -> 12.0 mm
- net PG_MODULE: track 0.00 -> 11.5 mm, vias 0 -> 1
- net MIO15: track 47.2 -> 57.8 mm
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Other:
- board size 78.5 x 106.9 mm -> 98.3 x 106.9 mm
- board text added: "Cysat 1 SDR Breakout Board Cardedge Adapter C.S.B.B.C.A"

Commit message: Completed routing and added gerber
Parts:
- added J5: IO_L Breakout, Pin_Headers:Pin_Header_Straight_1x10_Pitch2.54mm, F.Cu at (85.0, 104.0)
- moved J1 1.04 mm to (85.0, 101.1)
- moved J3 0.58 mm to (124.1, 65.7)
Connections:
- J1 pad 8: JX_MGTAVCC -> JX_MGTAVTT
- J1 pad 9: JX_MGTAVTT -> JX_MGTAVCC
- J3 pad 4: USB_OTG_CPEN -> GND
- J3 pad 6: Net-(J3-Pad6) -> USB_OTG_CPEN
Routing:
- net JX_VCCO_13: track 0.00 -> 103.9 mm, vias 0 -> 2
- net 3V3_I2C: track 0.00 -> 84.1 mm, vias 0 -> 4
- net JX_VCCO_33_34: track 0.00 -> 75.8 mm
- net JX_VCCO_12: track 0.00 -> 56.4 mm
- net JX_MGTAVTT: track 0.00 -> 32.6 mm
- net MIO12: track 45.2 -> 73.4 mm
- net JX_MGTAVCC: track 0.00 -> 27.6 mm
- net Net-(P7-Pad22): track 25.7 -> 0.00 mm
- net IO_L01_33_JX1_N: track 0.00 -> 24.9 mm, vias 0 -> 1
- net IO_L01_33_JX1_P: track 0.00 -> 23.5 mm, vias 0 -> 1
- net IO_L22_33_JX1_N: track 0.00 -> 23.4 mm, vias 0 -> 1
- net IO_L22_33_JX1_P: track 0.00 -> 22.5 mm, vias 0 -> 1
- net IO_L20_33_JX1_N: track 0.00 -> 20.9 mm, vias 0 -> 1
- net IO_L20_33_JX1_P: track 0.00 -> 20.2 mm, vias 0 -> 1
- net Net-(P7-Pad21): track 20.2 -> 0.00 mm
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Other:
- board text added: "CySat 1 - SDR Breakout Board"
- board text added: "JX1"
- board text added: "JX2"
- board text added: "JX3"
- board text added: "JX4"
